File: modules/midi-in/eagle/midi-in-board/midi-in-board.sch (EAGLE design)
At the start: 28 parts, among them IC1 LM358N, X1 POWER IN, X2 MIDI IN, X3 MIDI THRU, X4 CHANNEL SELECT SW, X5 22-23-2051, X6 POWER OUT CV

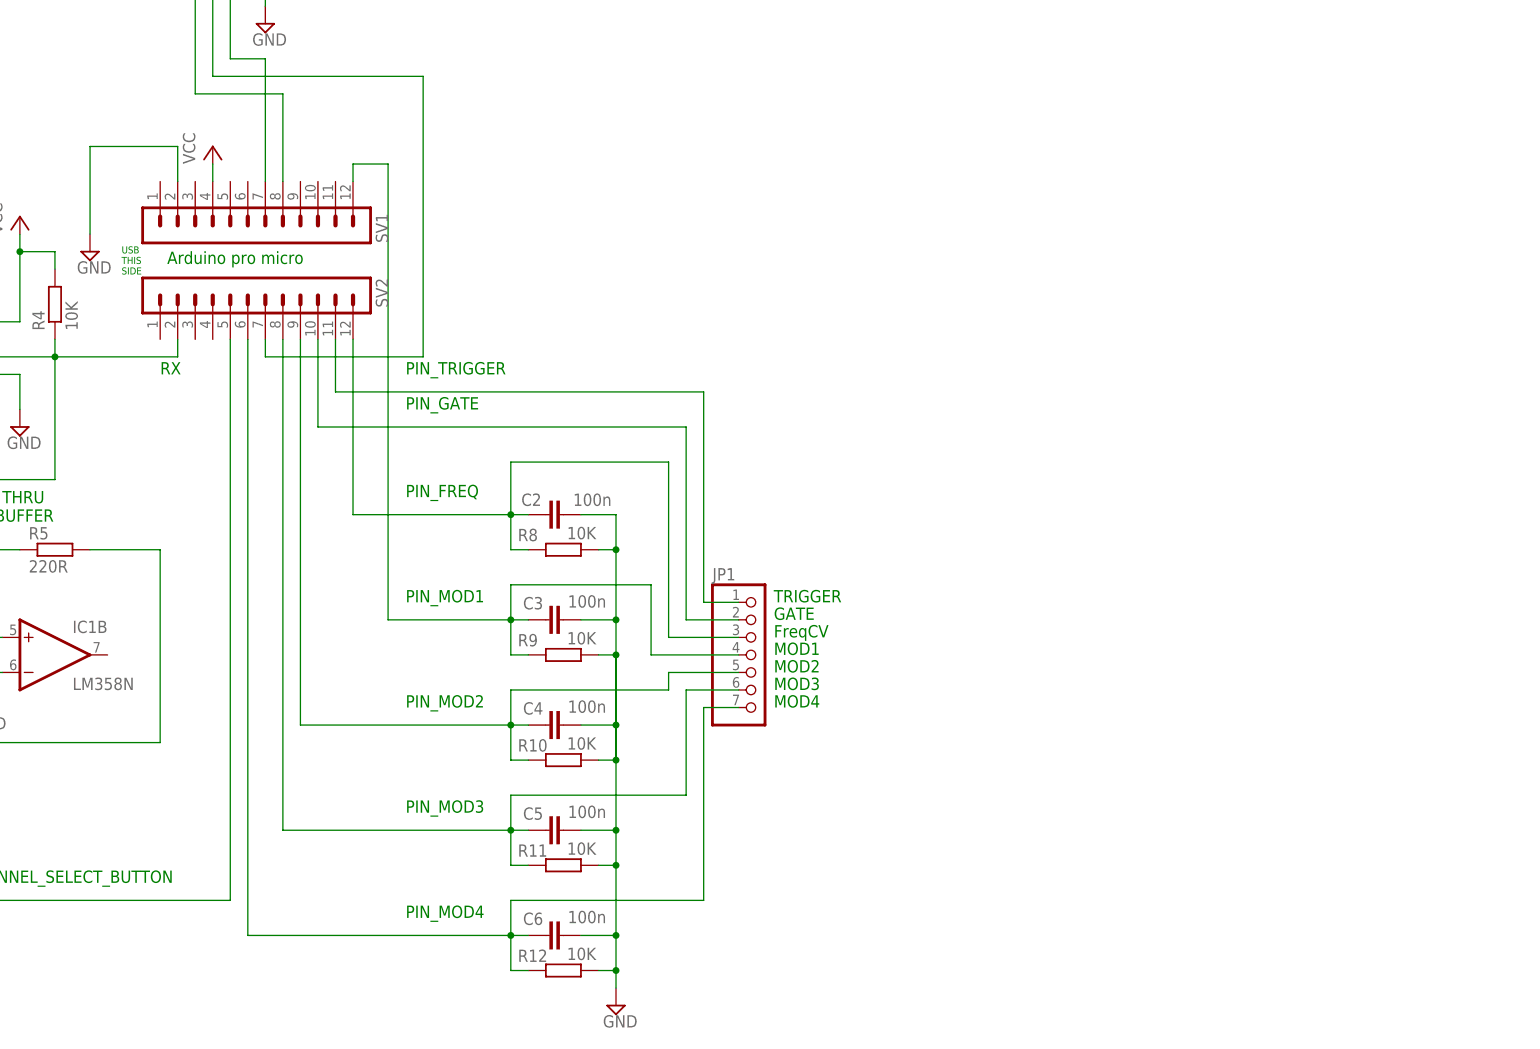
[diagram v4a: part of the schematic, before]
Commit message: Redesign of MIDI in board, now with DAC.
Remapped the names of DAC channels, for more straightforward PCB routing.
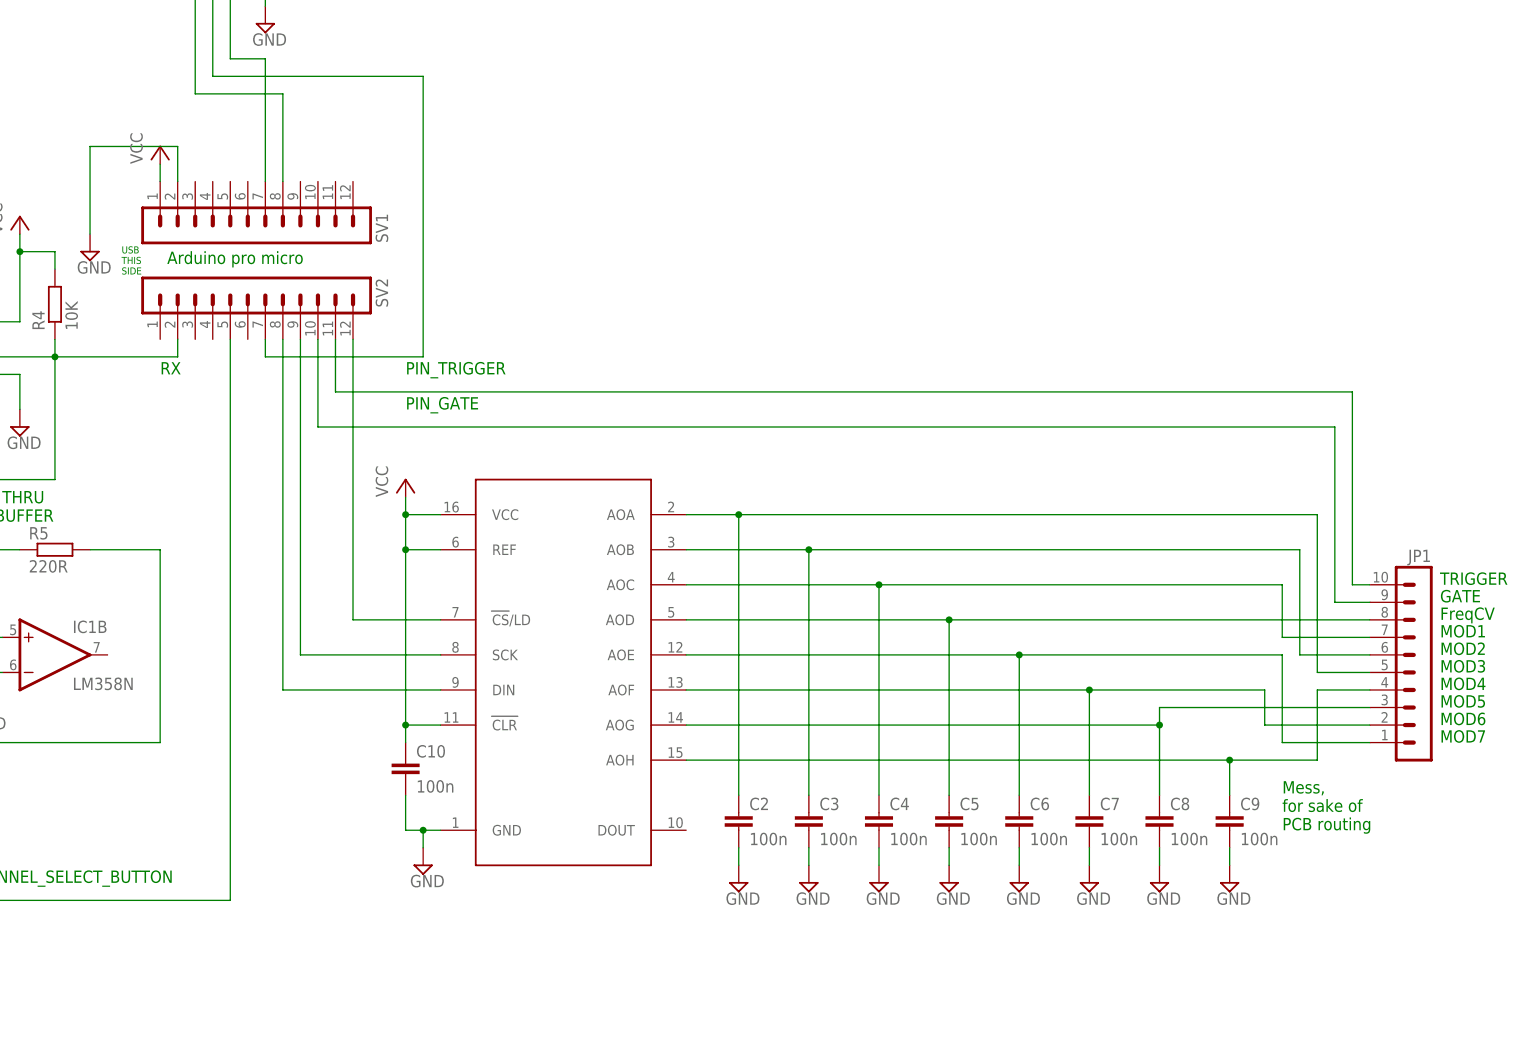
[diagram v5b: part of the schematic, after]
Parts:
- removed R10, R11, R12, R8, R9: 10K, rcl:R-EU_0207/7
- added C10, C7, C8, C9: 100n, rcl:C-EU050-024X044
- added U$1: LTC1660, LTC1660:LTC1660
- JP1: device pinhead:PINHD-1X7 -> con-lstb:MA10-1
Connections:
- removed net N$13: C2.1, JP1.3, R8.1, SV2.12
- removed net N$18: C6.1, JP1.7, R12.1, SV2.6
- removed net N$20: C3.1, JP1.4, R9.1, SV1.12
- new net N$22: C2.1, JP1.5, U$1.AOA
- new net N$23: SV2.12, U$1.CS/LD
- new net N$27: C3.1, JP1.6, U$1.AOB
- new net N$31: C6.1, JP1.1, U$1.AOE
- new net N$33: C4.1, JP1.7, U$1.AOC
- new net N$34: C5.1, JP1.8, U$1.AOD
- new net N$36: C7.1, JP1.2, U$1.AOF
- new net N$37: C8.1, JP1.3, U$1.AOG
- new net N$38: C9.1, JP1.4, U$1.AOH
- net GND: now also C10.2, C7.2, C8.2, C9.2, U$1.GND; no longer R10.2, R11.2, R12.2, R8.2, R9.2
- net N$11: now also JP1.10; no longer JP1.1
- net N$12: now also JP1.9; no longer JP1.2
- net N$16: now also U$1.SCK; no longer C4.1, JP1.5, R10.1
- net N$17: now also U$1.DIN; no longer C5.1, JP1.6, R11.1
- net VCC: now also C10.1, SV1.1, U$1.CLR, U$1.REF, U$1.VCC; no longer SV1.4
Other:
- note added: "MOD5"
- note added: "MOD6"
- note added: "MOD7"
- note added: "Mess, for sake of PCB routing"
- note removed: "PIN_FREQ"
- note removed: "PIN_MOD1"
- note removed: "PIN_MOD2"
- note removed: "PIN_MOD3"
- note removed: "PIN_MOD4"
- moved on the sheet: C2, C3, C4, C5, C6
